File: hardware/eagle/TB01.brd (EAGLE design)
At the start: 50 x 50 mm, 27 parts, among them J1 CON_TERMINAL_BLOCK_02-5MM, J4 CON_TERMINAL_BLOCK_02-5MM, J5 CON_TERMINAL_BLOCK_03-5MM, T1 BT138-V, T2 BT138-V

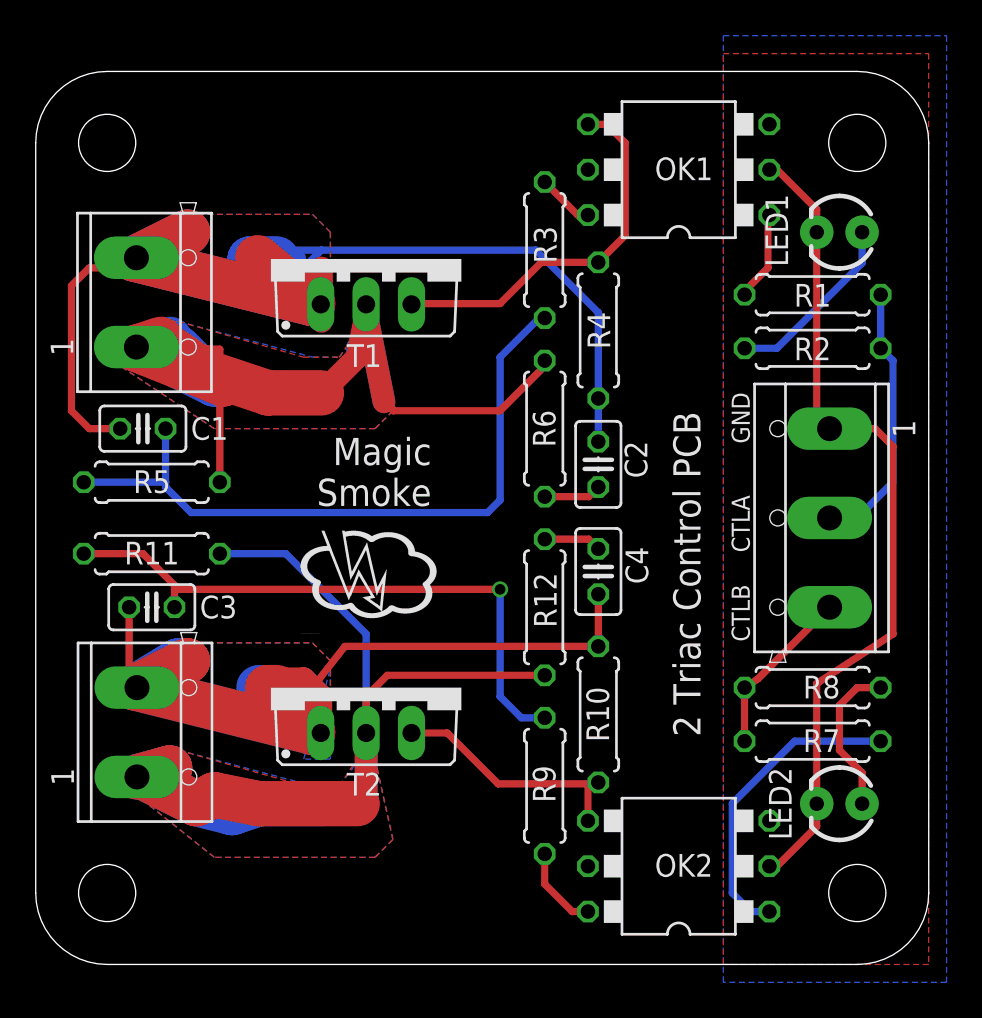
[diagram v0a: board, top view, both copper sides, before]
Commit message: layout altered, resistor values
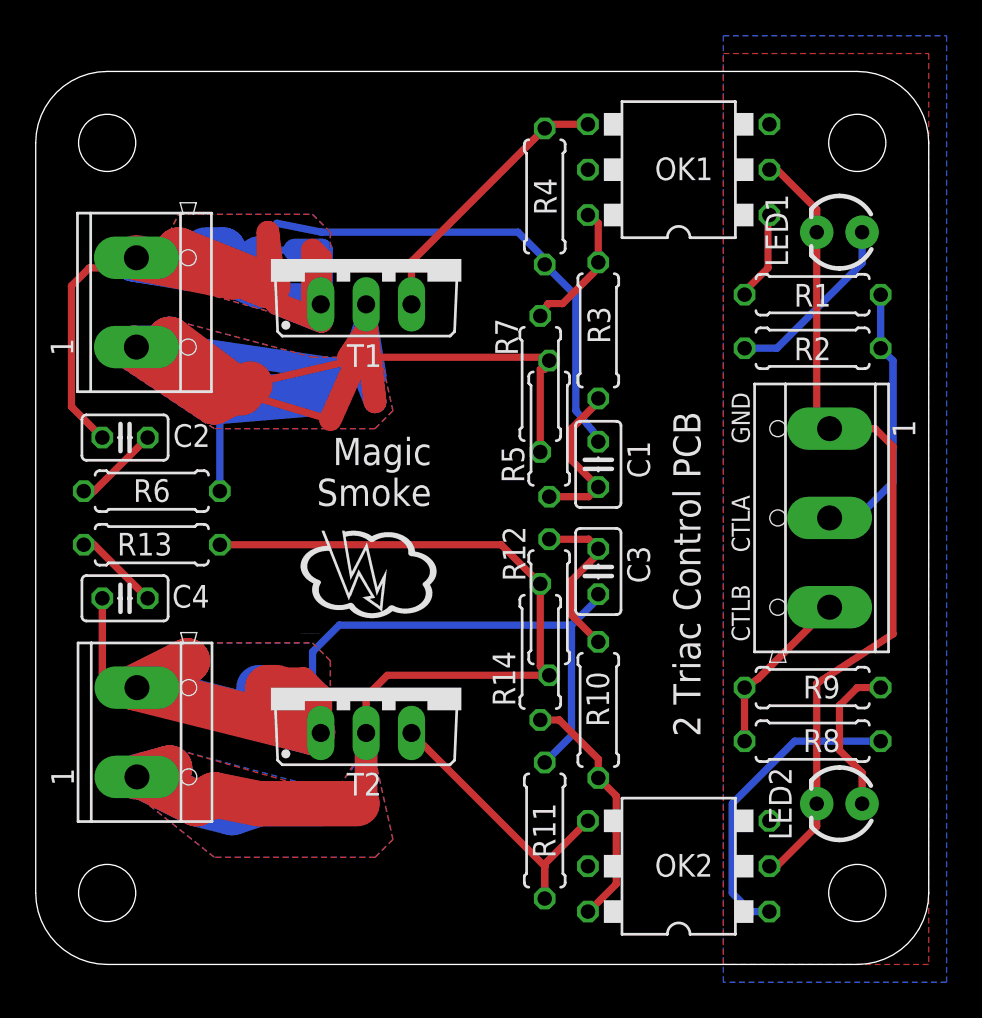
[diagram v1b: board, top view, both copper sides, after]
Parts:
- added R13: 39R, rcl:0207/7
- added R14: 360R, rcl:0207/7
- C2, C4: value (none) -> 10 nF
- R1, R8: value (none) -> 150R
- R11, R4: value (none) -> 330R
- R2, R9: value (none) -> 1K
- R6: value (none) -> 39R
- R7: value (none) -> 360R
- moved R11 26.9 mm to (28.5, 7.50), turned to 90 degrees
- moved C2 26.5 mm to (5.00, 29.5), turned to 180 degrees
- moved C4 26.5 mm to (5.00, 20.5), turned to 180 degrees
- moved C1 25.6 mm to (31.5, 28.0), turned to 90 degrees
- moved R7 25.2 mm to (28.2, 32.5), turned to 270 degrees
- moved C3 25.1 mm to (31.5, 22.0), turned to 270 degrees
- moved R5 22.5 mm to (28.8, 30.0), turned to 90 degrees
- moved R6 22.3 mm to (6.50, 26.5), turned to 0 degrees
- moved R9 16.0 mm to (43.5, 15.5), turned to 0 degrees
- moved R4 8.08 mm to (28.5, 43.0)
- moved R3 5.41 mm to (31.5, 35.5)
- moved R8 3.00 mm to (43.5, 12.5)
- moved R10 0.25 mm to (31.5, 14.2)
- moved R12 0.25 mm to (28.8, 20.0)
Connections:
- net CTLB: now also R9.1; no longer R7.1
- net LOAD_A1: now also R7.2
- net LOAD_B1: now also R13.2, R14.2; no longer R11.2
- net LOAD_B2: now also R11.2; no longer R10.2
- net N$10: now also R10.2, R12.1; no longer R11.1, R9.2
- net N$11: now also R13.1; no longer R12.1
- net N$12: now also R11.1; no longer R10.1
- net N$3: now also R7.1
- net N$6: now also R9.2; no longer R8.2
- net N$8: now also R8.2; no longer R7.2
- net N$9: now also R10.1, R14.1; no longer R9.1
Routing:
- net LOAD_A1: track 76.4 -> 121.6 mm
- net N$4: track 38.9 -> 9.18 mm
- net N$10: track 34.3 -> 9.43 mm, vias 1 -> 0
- net LOAD_B2: track 74.6 -> 87.8 mm
- net N$9: track 4.75 -> 13.8 mm
- net LOAD_B1: track 66.4 -> 75.3 mm
- net LOAD_A2: track 98.6 -> 105.4 mm
- net N$5: track 21.3 -> 15.5 mm
- net N$3: track 3.19 -> 7.73 mm
- net N$12: track 13.7 -> 17.7 mm
- net N$7: track 3.22 -> 4.82 mm
- net N$11: track 3.22 -> 4.82 mm

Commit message: high voltage warning
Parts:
- moved U$2 7.80 mm to (17.5, 25.0)
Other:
- board text added: "DANGER"
- board text added: "HIGH VOLTAGE"
- board text added: "LOAD A"
- board text added: "LOAD B"
- board text removed: "Magic Smoke"

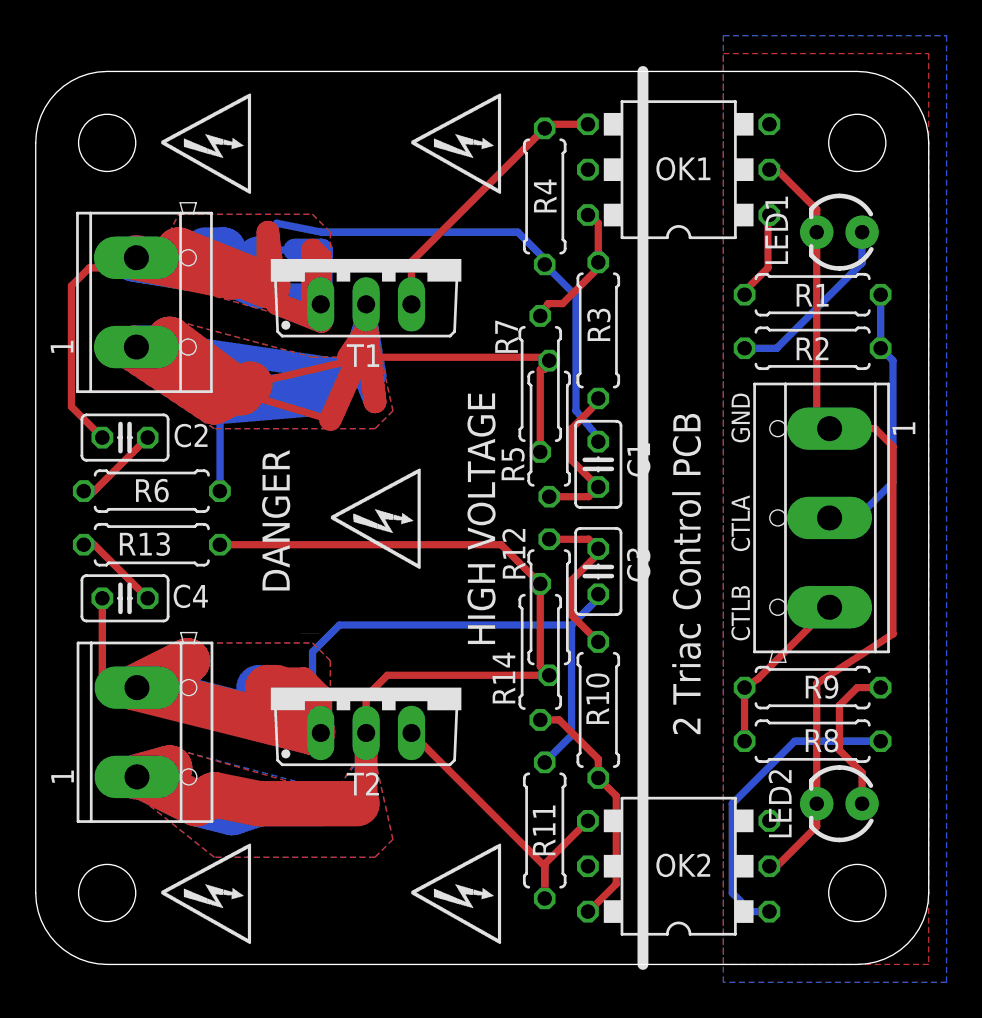
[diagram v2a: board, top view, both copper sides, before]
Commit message: redesign without snubbers
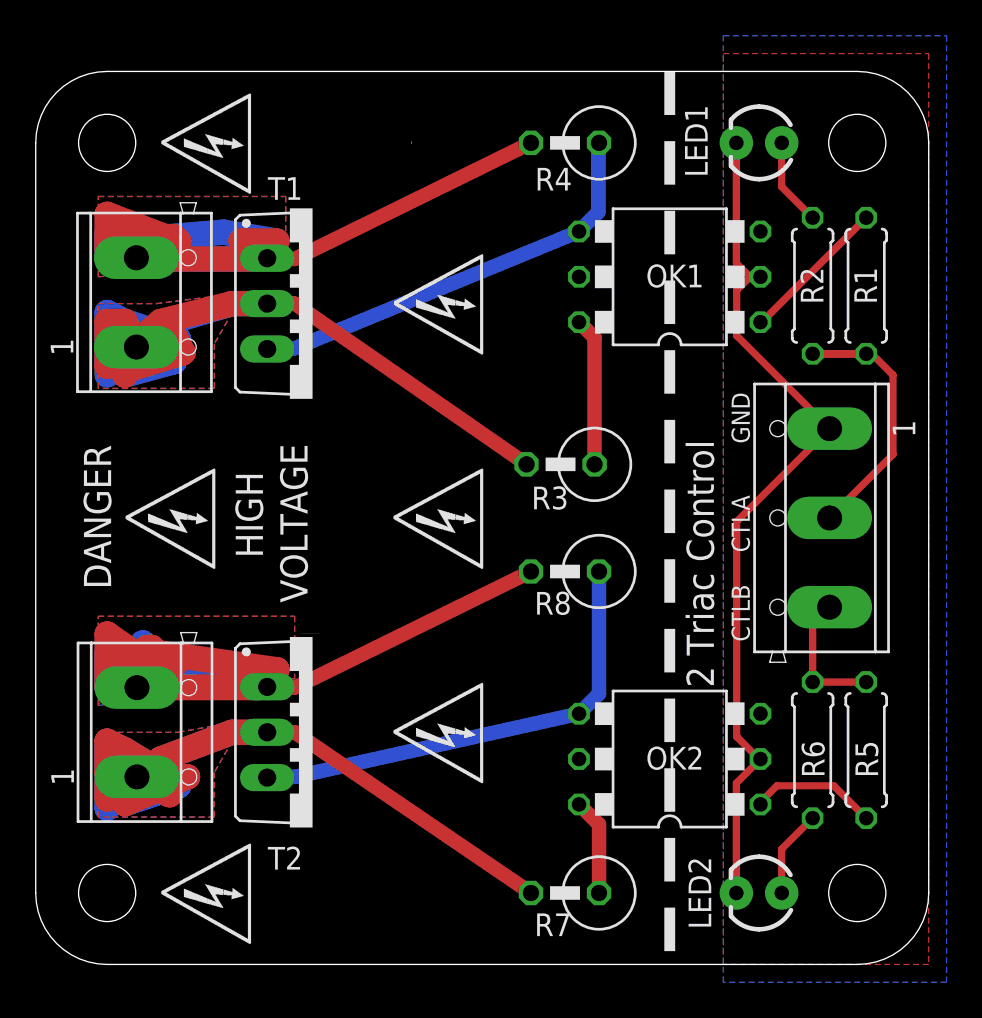
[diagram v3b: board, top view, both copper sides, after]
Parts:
- removed C1, C3: (no value), rcl:C025-025X050
- removed C2, C4: 10 nF, rcl:C025-025X050
- removed J4: CON_TERMINAL_BLOCK_02-5MM, dp_devices:TERMINAL_BLOCK_2P_5
- removed R10, R12: (no value), rcl:0207/7
- removed R11: 330R, rcl:0207/7
- removed R13: 39R, rcl:0207/7
- removed R14: 360R, rcl:0207/7
- removed R9: 1K, rcl:0207/7
- added J2: CON_TERMINAL_BLOCK_02-5MM, dp_devices:TERMINAL_BLOCK_2P_5
- R3: value (none) -> 360R 0.5W; device rcl:0207/7 -> rcl:0411V
- R4: value 330R -> 330R 0.5W; device rcl:0207/7 -> rcl:0411V
- R5: value (none) -> 150R
- R6: value 39R -> 1K
- R7: value 360R -> 360R 0.5W; device rcl:0207/7 -> rcl:0411V
- R8: value 150R -> 330R 0.5W; device rcl:0207/7 -> rcl:0411V
- T1, T2: value BT138-V -> BTA16-600W
- moved R6 39.7 mm to (43.5, 12.0), turned to 270 degrees
- moved R7 28.5 mm to (29.0, 4.00), turned to 180 degrees
- moved R5 25.3 mm to (46.5, 12.0), turned to 270 degrees
- moved J1 24.1 mm to (6.09, 37.1)
- moved R8 17.3 mm to (29.0, 22.0), turned to 180 degrees
- moved R3 7.99 mm to (28.8, 28.0), turned to 180 degrees
- moved LED1 6.73 mm to (40.5, 46.0)
- moved LED2 6.73 mm to (40.5, 4.00)
- moved OK1 6.02 mm to (35.5, 38.5)
- moved OK2 6.02 mm to (35.5, 11.5)
- moved U$2 6.00 mm to (11.5, 25.0)
- moved T1 3.91 mm to (15.5, 37.0), turned to 270 degrees
- moved T2 3.91 mm to (15.5, 13.0), turned to 270 degrees
- moved R2 3.50 mm to (43.5, 38.0), turned to 90 degrees
- moved R1 3.04 mm to (46.5, 38.0), turned to 90 degrees
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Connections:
- removed net N$10: C3.1, R10.2, R12.1
- removed net N$11: C4.1, R13.1
- removed net N$12: OK2.4, R11.1, T2.G
- removed net N$9: OK2.6, R10.1, R14.1
- net CTLB: now also R5.1, R6.1; no longer R8.1, R9.1
- net LOAD_A1: now also J1.1, R3.2; no longer J4.1, R5.2, R6.2, R7.2
- net LOAD_A2: now also J1.2; no longer C1.2, C2.2, J4.2
- net LOAD_B1: now also J2.1, R7.2; no longer J1.1, R12.2, R13.2, R14.2
- net LOAD_B2: now also J2.2, R8.2; no longer C3.2, C4.2, J1.2, R11.2
- net N$3: no longer R7.1
- net N$4: now also OK2.6, R7.1; no longer C1.1, R3.2, R5.1
- net N$6: now also R6.2; no longer R9.2
- net N$7: now also OK2.4, R8.1, T2.G; no longer C2.1, R6.1
- net N$8: now also R5.2; no longer R8.2
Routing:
- net LOAD_A1: track 121.6 -> 73.5 mm
- net LOAD_A2: track 105.4 -> 68.7 mm
- net N$7: track 4.82 -> 26.3 mm
- net N$12: track 17.7 -> 0.00 mm
- net N$9: track 13.8 -> 0.00 mm
- net N$8: track 17.3 -> 7.17 mm
- net N$10: track 9.43 -> 0.00 mm
- net N$5: track 15.5 -> 24.2 mm
- net N$1: track 10.3 -> 4.91 mm
- net N$11: track 4.82 -> 0.00 mm
- net N$6: track 8.75 -> 4.91 mm
- net N$4: track 9.18 -> 5.42 mm
- net LOAD_B1: track 75.3 -> 71.7 mm
- net N$2: track 5.04 -> 8.34 mm
- net CTLA: track 15.2 -> 17.5 mm
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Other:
- board text added: "2 Triac Control"
- board text added: "HIGH"
- board text added: "VOLTAGE"
- board text removed: "2 Triac Control PCB"

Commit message: splay pin triac package
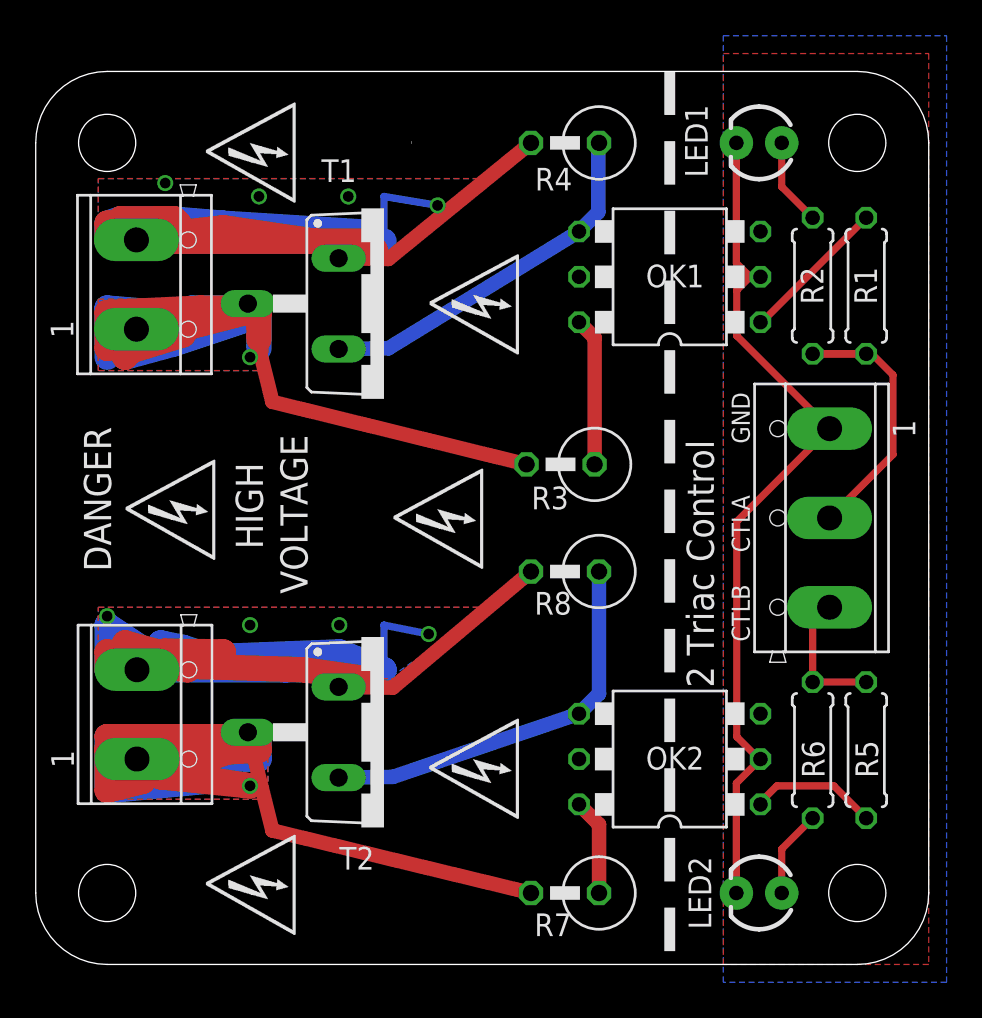
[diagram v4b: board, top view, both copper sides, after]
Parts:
- T1, T2: device triac:TO220BV -> triac:TO220DSH
- moved T1 4.00 mm to (19.5, 37.0)
- moved T2 4.00 mm to (19.5, 13.0)
- moved J1 1.00 mm to (6.09, 38.1)
- moved J2 1.00 mm to (6.12, 14.0)
- moved U$2 0.50 mm to (11.5, 25.5)
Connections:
- net LOAD_A1: now also T1.A2; no longer T1.T2
- net LOAD_A2: now also T1.A1; no longer T1.T1
- net LOAD_B1: now also T2.A2; no longer T2.T2
- net LOAD_B2: now also T2.A1; no longer T2.T1
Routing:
- net LOAD_B1: track 71.7 -> 156.6 mm, vias 0 -> 1
- net LOAD_A1: track 73.5 -> 129.0 mm, vias 0 -> 1
- net LOAD_B2: track 89.6 -> 127.2 mm, vias 0 -> 4
- net LOAD_A2: track 68.7 -> 100.3 mm, vias 0 -> 4
- net N$7: track 26.3 -> 22.5 mm
- net N$5: track 24.2 -> 20.7 mm
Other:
- board text removed: "/Users/thomasprice/Documents/eagle/logo/Magic_Smoke_logo.bmp"
